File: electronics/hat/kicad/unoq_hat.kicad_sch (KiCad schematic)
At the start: 87 parts, among them J1 JMEDIA 2x30 1.27 SMD male (GP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, J10 SM02B-SRSS-TB left foot conta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, J11 SM02B-SRSS-TB right foot cont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, J12 BM04B-SRSS-TB trunk IMU I2C, J2 JMISC 2x30 1.27 SMD male (GPE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, J3 TF31-22S-0.5SH 22p 0.5 FFC (I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, J4 BM06B-SRSS-TB ToF, J5 S3B-PH-SM4-TB servo bus, J6 S4B-PH-SM4-TB 2S pack in, J7 S2B-PH-SM4-TB speaker, J8 SM02B-SRSS-TB electret mic, J9 SM02B-SRSS-TB touch pad, Q1 MMBT3906, Q2 AON6407 reverse-polarity P-FET, U1 TCA9406DCUR, U2 TCA9555PWR, U3 TPS62933DRLR, U4 PAM8302AASCR, U5 SN74LVC1G126DBVR, U6 SN74LVC1G125DBVR, U7 LSM6DSV16X, U8 INA226AIDGSR, U9 TTP233H-BA6

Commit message: hat rev C: boost to UNO Q VIN, EN divider fix, checks and docs
Rev C of the UNO Q head hat (foreman/microduck-assembly.60, 2026-10-10):
- TPS61088 boost (U10) makes 11.86 V from the 2S pack into the UNO Q VIN
  (JMEDIA 57/59); the hat no longer back-feeds the UNO Q 5 V.
- U10 EN now sits on a 100k/100k divider from VBAT_B. Earlier Rev C builds
  tied EN to VCC, the output of an LDO that EN itself enables, so the boost
  would never have started. DRC and ERC could not see it.
- Interrupts on 3.3 V MCU pins, D40 isolates the servo pull-ups.
- kicad_dru no longer carries a 0.09 mm clearance rule: it replaced the
  0.127 mm zone clearance and filled GND inside the JMEDIA mask openings.

Checks: kicad-cli DRC 0 errors / 0 warnings / 0 unconnected (board rules and
JLC rules), ERC 0/0, schematic vs board 75/75 nets. Docs: footprint table
(51 parts), strap pins (29 rows), power budget, BOM with live stock.

Co-Authored-By: Claude Opus 5.5 <noreply@anthropic.com>
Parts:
- added C30, C31, C37, C38, C39: 22uF 25V, Capacitor_SMD:C_1210_3225Metric, symbol Device:C
- added C32, C34: 100nF 25V, Capacitor_SMD:C_0402_1005Metric, symbol Device:C
- added C33: 4.7uF 16V, Capacitor_SMD:C_0603_1608Metric, symbol Device:C
- added C35: 47nF, Capacitor_SMD:C_0402_1005Metric, symbol Device:C
- added C36: 6.8nF, Capacitor_SMD:C_0402_1005Metric, symbol Device:C
- added D40: BAT54H,115, unoq_hat:BAT54H_Nexperia_SOD123F, symbol Device:D_Schottky
- added F2: JK-MSMD500L-12V 5A PTC, Fuse:Fuse_1812_4532Metric, symbol Device:Fuse
- added L2: FXL0630-2R2-M 2.2uH, Inductor_SMD:L_Changjiang_FXL0630, symbol Device:L
- added R30: 300k, Resistor_SMD:R_0402_1005Metric, symbol Device:R
- added R31: 150k, Resistor_SMD:R_0402_1005Metric, symbol Device:R
- added R32: 1M, Resistor_SMD:R_0402_1005Metric, symbol Device:R
- added R33: 113k, Resistor_SMD:R_0402_1005Metric, symbol Device:R
- added R34: 18k, Resistor_SMD:R_0402_1005Metric, symbol Device:R
- added R35, R36: 100k, Resistor_SMD:R_0402_1005Metric, symbol Device:R
- added TP7: VIN12, TestPoint:TestPoint_Pad_D1.0mm, symbol Connector:TestPoint
- added U10: TPS61088RHLR, Package_DFN_QFN:Texas_VQFN-RHL-20, symbol local:TPS61088
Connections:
- net +3V3: now also D40.2 (A); no longer R15.2, R21.2
- net EXP_INT: now also J2.7 (Pin_7); no longer J2.39 (Pin_39)
- net GND: now also C30.2, C31.1, C32.2, C33.2, C35.2, C36.2, C37.2, C38.2, C39.2, R31.2, R33.2, R36.1, U10.11 (NC), U10.12 (NC), U10.20 (AGND), U10.21 (PGND)
- net IMU_INT1: now also J2.3 (Pin_3); no longer J2.37 (Pin_37)
- net INA_ALERT: now also J2.9 (Pin_9); no longer J2.41 (Pin_41)
- net V5: no longer J2.54 (Pin_54), J2.56 (Pin_56)
- net VBAT: now also F2.1
- net VIN12: now reaches J1.57 (Pin_57)
- net VIN12: now also J1.59 (Pin_59), C37.1, C38.1, C39.1, R32.1, TP7.1, U10.14 (VOUT), U10.15 (VOUT), U10.16 (VOUT)
- new net BST_BOOT: C34.1, U10.8 (BOOT)
- new net BST_COMP: R34.1, U10.18 (COMP)
- new net BST_COMPRC: C36.1, R34.2
- new net BST_EN: R35.1, R36.2, U10.2 (EN)
- new net BST_FB: R32.2, R33.1, U10.17 (FB)
- new net BST_FSW: R30.1, U10.3 (FSW)
- new net BST_ILIM: R31.1, U10.19 (ILIM)
- new net BST_SS: C35.1, U10.10 (SS)
- new net BST_VCC: C33.1, U10.1 (VCC)
- new net SERVO_PULLUP: D40.1 (K), R15.2, R21.2
- new net SW2: C34.2, L2.2, R30.2, U10.4 (SW), U10.5 (SW), U10.6 (SW), U10.7 (SW)
- new net VBAT_B: C30.1, C31.2, C32.1, F2.2, L2.1, R35.2, U10.9 (VIN)
- no-connect marks 75 -> 76
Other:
- note added: "UNO Q VIN BOOST"
- note added: "UNO Q head hat rev B. Board-to-board pinout and the camera block copied from Arduino's UNO Media Carrier ASX00083 so arduino-linux-config camera0=type1-2lanes applies. 2S pack -> 5 mOhm shunt -> AON6407. PTC F2 -> TPS61088 11.9 V -> JMEDIA 57/59 VIN (UNO Q's own buck). PTC F1 -> TPS62933 5 V -> amplifier only; JMISC 54/56 open. Interrupts on 3.3 V MCU pins J2.3/7/9. D40 keeps the servo pull-ups o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"
- note removed: "UNO Q head hat rev B. Board-to-board pinout and the camera block copied from Arduino's UNO Media Carrier ASX00083 so arduino-linux-config camera0=type1-2lanes applies. 2S pack -> 5 mOhm shunt -> AON6407 -> PTC -> TPS62933 5 V -> JMISC 5V_SYS. One 3.3 V I2C bus (CCI0) carries camera 0x10, expander 0x26, ToF 0x29, INA226 0x40, head IMU 0x6B and, on J12, the trunk IMU 0x6A."
- moved on the sheet: C10, C11, C12, C13, C14, C15, C16, C19, C2, C20, C21, C22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

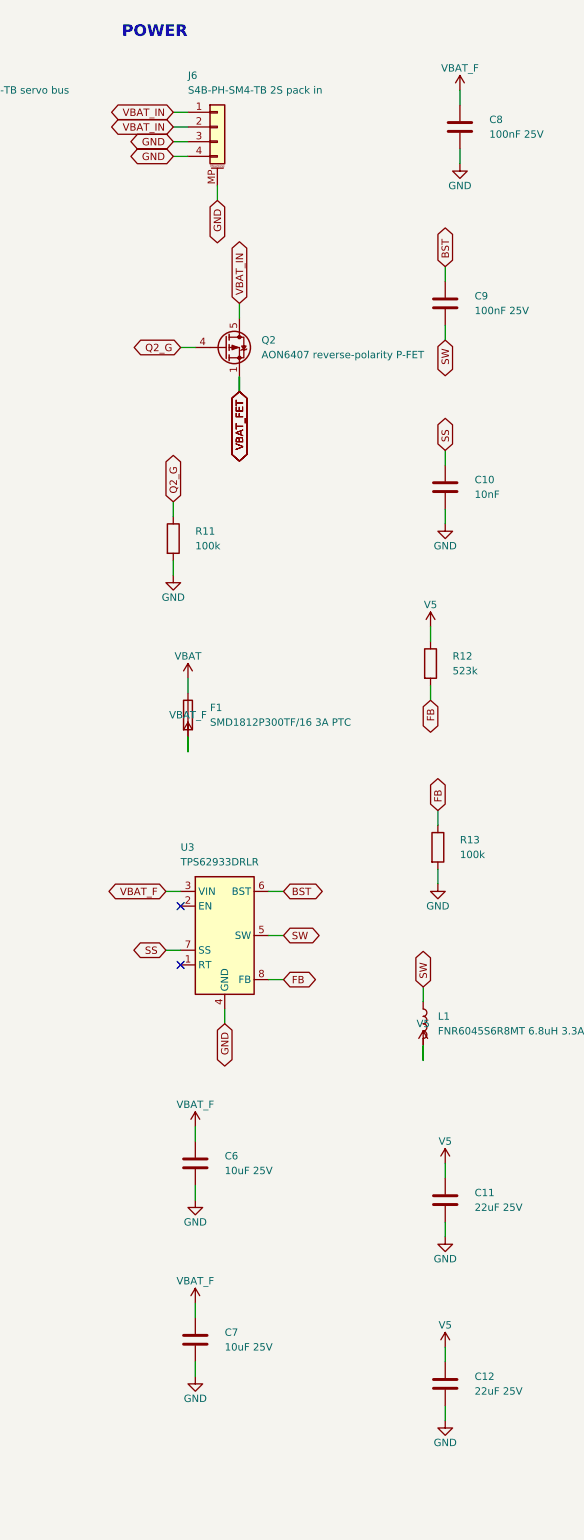
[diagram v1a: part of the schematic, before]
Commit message: hat Rev C build #10: 6-pin J6 (6 A), order sheet for 2026-10-11
- J6 is now S6B-PH-SM4-TB (C265405), three contacts per pole: 6 A vs 4.72 A worst case
- VBAT_IN pour widened for J6; KiCad DRC 0/0/0 (board and JLC rules), ERC 0/0, 75/75 nets
- fab: gerbers.zip, bom.csv (55 lines), cpl.csv (95 parts); BOM in stock for 5 boards at 14:53Z
- ce-fabmcp pcb_drc on build #10: In1/In2 PASS, F/B approximation FAIL explained
- docs/PCB-ORDER-LEIF-2026-10-11.md: one-page order sheet with J6-to-XT30 pigtail kit line

Signed: foreman/microduck-assembly.60

Co-Authored-By: Claude Opus 5.5 <noreply@anthropic.com>
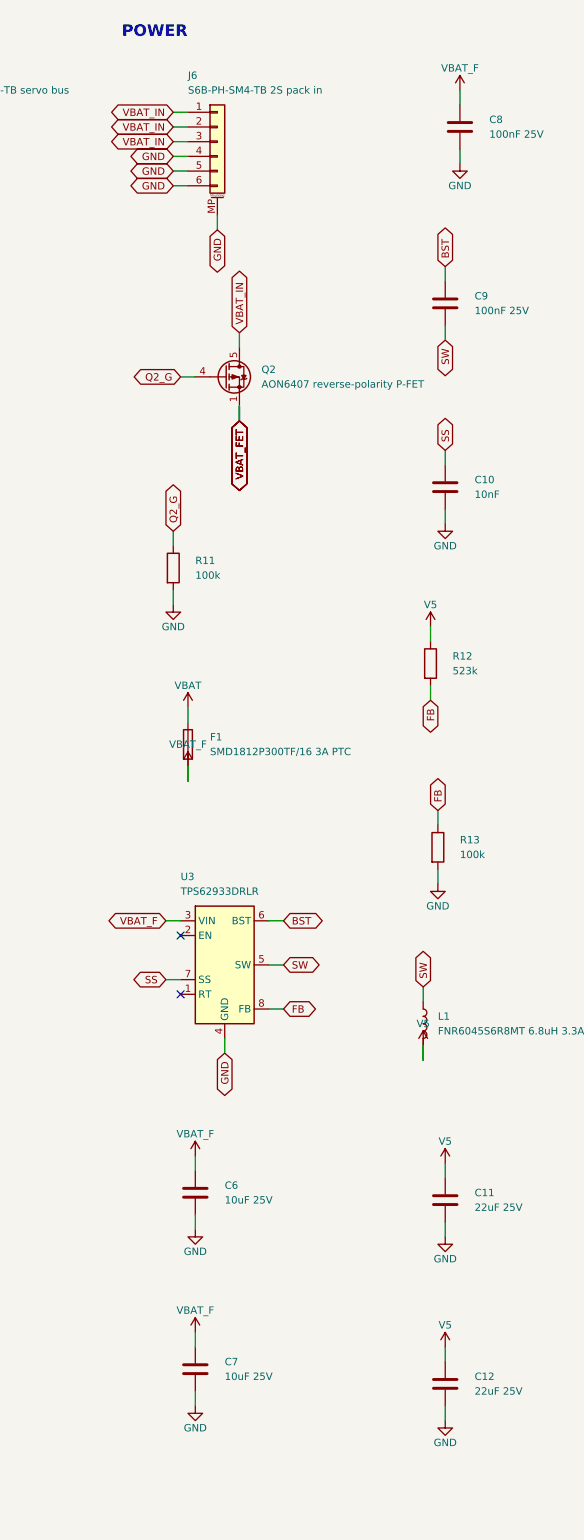
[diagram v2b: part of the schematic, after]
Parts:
- J6: value S4B-PH-SM4-TB 2S pack in -> S6B-PH-SM4-TB 2S pack in; footprint Connector_JST:JST_PH_S4B-PH-SM4-TB_1x04-1MP_P2.00mm_Horizontal -> Connector_JST:JST_PH_S6B-PH-SM4-TB_1x06-1MP_P2.00mm_Horizontal; symbol Connector_Generic_MountingPin:Conn_01x04_MountingPin -> Connector_Generic_MountingPin:Conn_01x06_MountingPin; LCSC Part # C265102 -> C265405
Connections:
- net GND: now also J6.5 (Pin_5), J6.6 (Pin_6); no longer J6.3 (Pin_3)
- net VBAT_IN: now also J6.3 (Pin_3)
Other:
- moved on the sheet: C6, C7, F1, Q2, R11, U3
